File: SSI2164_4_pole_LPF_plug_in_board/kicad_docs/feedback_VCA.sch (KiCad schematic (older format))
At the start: 23 parts, among them Q3 BCM847DS135, Q4 MMBT3904, Q5 MMBT3904, Q6 MMBT3906, U5 TL072

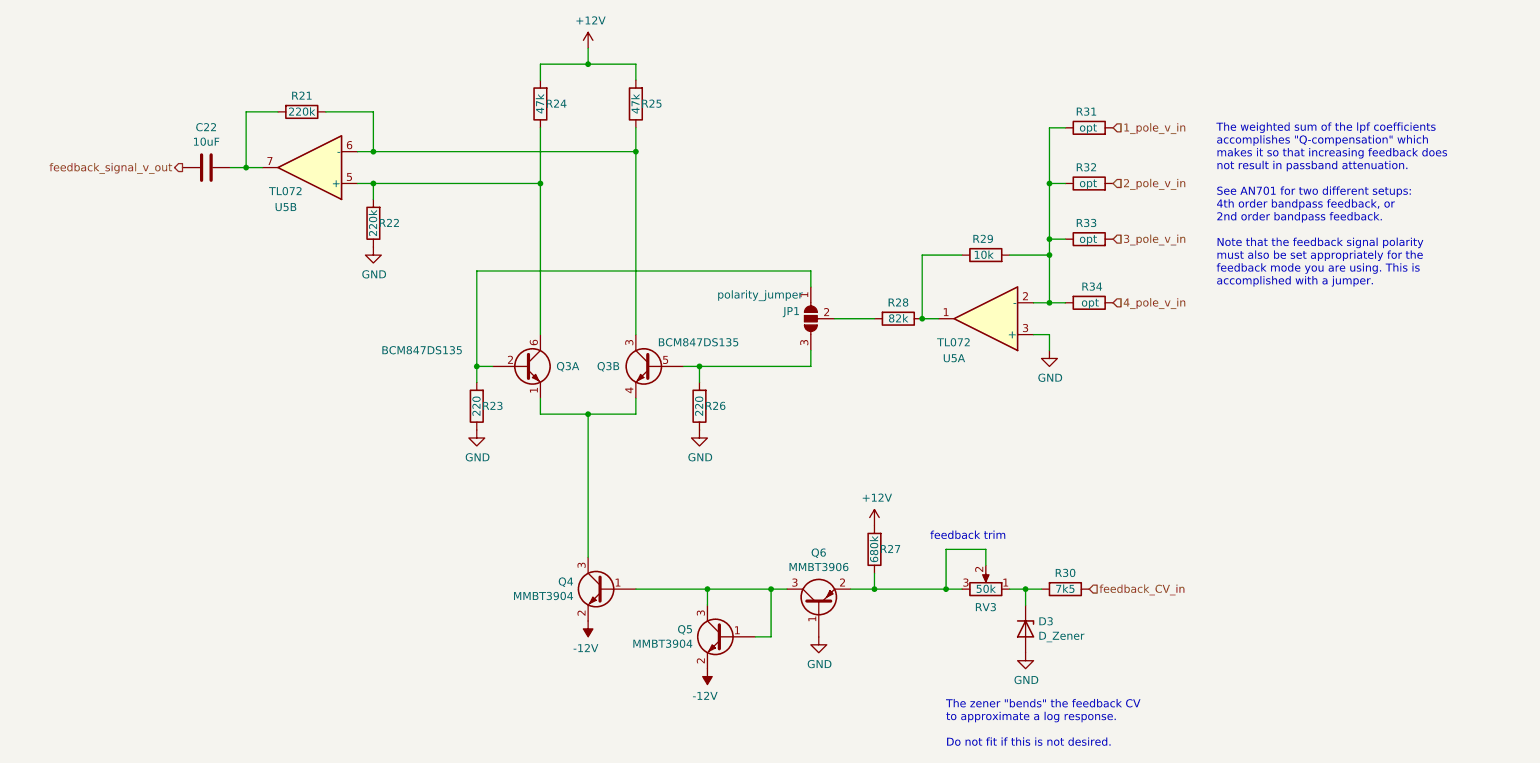
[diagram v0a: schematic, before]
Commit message: progress on SSI2164 LPF
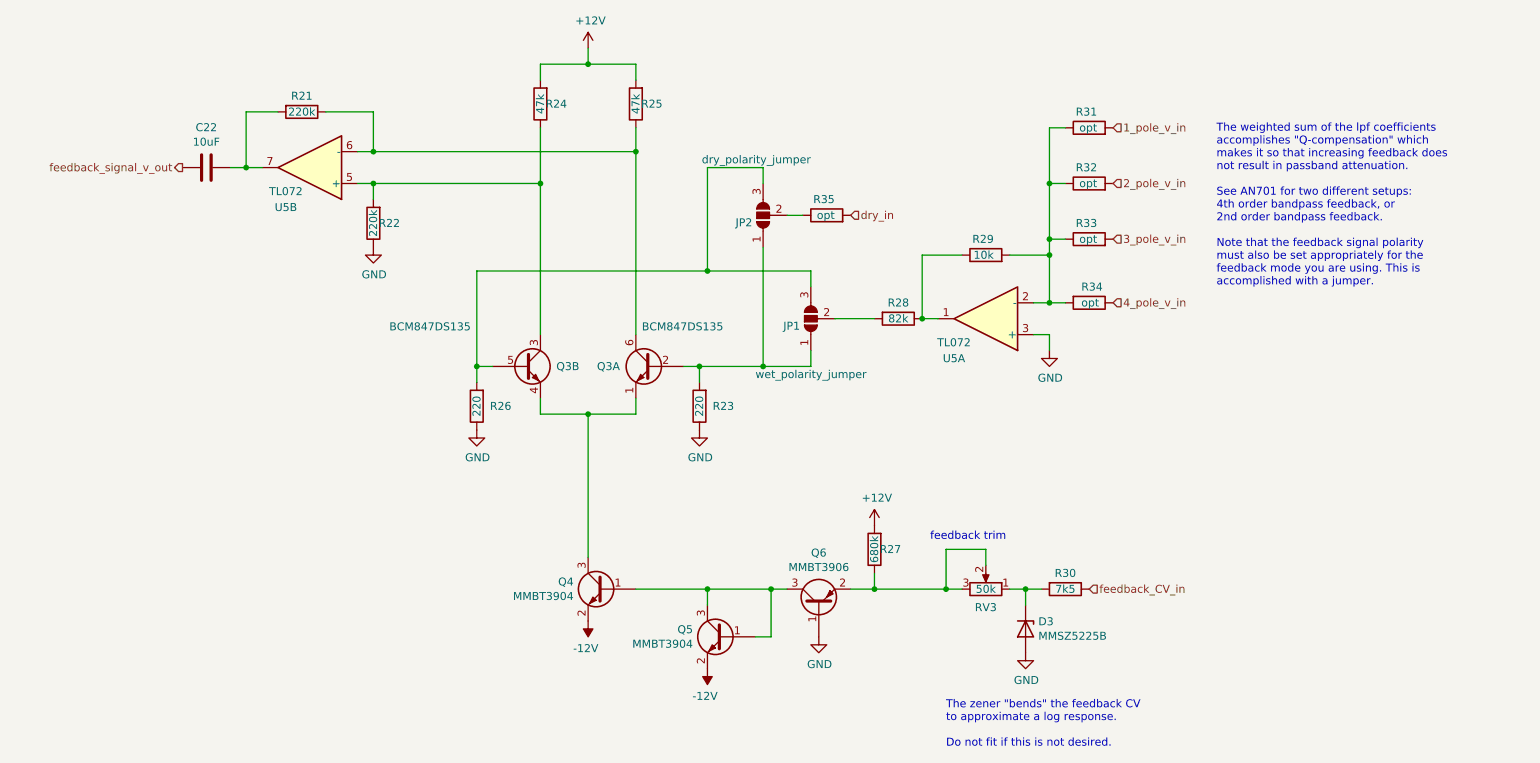
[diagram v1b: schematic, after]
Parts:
- added JP2: dry_polarity_jumper, Jumper:SolderJumper-3_P1.3mm_Open_RoundedPad1.0x1.5mm, symbol Jumper:SolderJumper_3_Open
- added R35: opt, Resistor_SMD:R_0805_2012Metric_Pad1.15x1.40mm_HandSolder, symbol Device:R
- C22: footprint Capacitor_THT:CP_Radial_D6.3mm_P2.50mm -> Capacitor_THT:C_Radial_D6.3mm_H5.0mm_P2.50mm
- D3: value D_Zener -> MMSZ5225B
- JP1: value polarity_jumper -> wet_polarity_jumper
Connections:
- net at R22.2, R24.1, U5.5 (+): now also Q3.3 (C); no longer Q3.6 (C)
- net at R21.1, R25.1, U5.6 (-): now also Q3.6 (C); no longer Q3.3 (C)
- net at JP1.1 (A), Q3.2 (B), R23.2: now also JP2.1 (A)
- net at JP1.3 (B), Q3.5 (B), R26.2: now also JP2.3 (B)
- new net: JP2.2 (C), R35.1
- new net dry_in: R35.2
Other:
- moved on the sheet: Q3A, Q3B, R23, R26
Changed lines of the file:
@@
 L Device:R R23
 U 1 1 5F0EDC2E
-P 4000 3700
-F 0 "R23" H 3900 3700 50  0000 C CNN
-F 1 "220" V 4000 3700 50  0000 C CNN
-F 2 "Resistor_SMD:R_0805_2012Metric_Pad1.15x1.40mm_HandSolder" V 3930 3700 50  0001 C CNN
-F 3 "~" H 4000 3700 50  0001 C CNN
-	1    4000 3700
+P 5400 3700
+F 0 "R23" H 5250 3700 50  0000 C CNN
+F 1 "220" V 5400 3700 50  0000 C CNN
+F 2 "Resistor_SMD:R_0805_2012Metric_Pad1.15x1.40mm_HandSolder" V 5330 3700 50  0001 C CNN
+F 3 "~" H 5400 3700 50  0001 C CNN
+	1    5400 3700
 	-1   0    0    1
 $EndComp
@@
 L Device:R R26
 U 1 1 5F0EEFAD
-P 5400 3700
-F 0 "R26" H 5300 3700 50  0000 C CNN
-F 1 "220" V 5400 3700 50  0000 C CNN
-F 2 "Resistor_SMD:R_0805_2012Metric_Pad1.15x1.40mm_HandSolder" V 5330 3700 50  0001 C CNN
-F 3 "~" H 5400 3700 50  0001 C CNN
-	1    5400 3700
+P 4000 3700
+F 0 "R26" H 3850 3700 50  0000 C CNN
+F 1 "220" V 4000 3700 50  0000 C CNN
+F 2 "Resistor_SMD:R_0805_2012Metric_Pad1.15x1.40mm_HandSolder" V 3930 3700 50  0001 C CNN
+F 3 "~" H 4000 3700 50  0001 C CNN
+	1    4000 3700
 	-1   0    0    1
 $EndComp
@@
 P 7450 5100
 F 0 "D3" V 7404 5180 50  0000 L CNN
-F 1 "D_Zener" V 7495 5180 50  0000 L CNN
+F 1 "MMSZ5225B" V 7495 5180 50  0000 L CNN
 F 2 "Diode_SMD:D_SOD-123" H 7450 5100 50  0001 C CNN
 F 3 "~" H 7450 5100 50  0001 C CNN
@@
 L lpf_parts:BCM847DS135 Q3
 U 1 1 5F114A19
+P 5100 3450
+F 0 "Q3" H 5300 3450 50  0000 L CNN
+F 1 "BCM847DS135" H 4650 3700 50  0000 L CNN
+F 2 "lpf_footprints:SOT457" H 5300 3375 50  0001 L CIN
+F 3 "" H 5100 3450 50  0001 L CNN
+	1    5100 3450
+	-1   0    0    -1
+$EndComp
+$Comp
+L lpf_parts:BCM847DS135 Q3
+U 2 1 5F12DDB3
 P 4300 3450
 F 0 "Q3" H 4500 3450 50  0000 L CNN
-F 1 "BCM847DS135" H 3400 3550 50  0000 L CNN
+F 1 "BCM847DS135" H 3450 3700 50  0000 L CNN
 F 2 "lpf_footprints:SOT457" H 4500 3375 50  0001 L CIN
 F 3 "" H 4300 3450 50  0001 L CNN
-	1    4300 3450
-	1    0    0    -1
-$EndComp
-$Comp
-L lpf_parts:BCM847DS135 Q3
-U 2 1 5F12DDB3
-P 5100 3450
-F 0 "Q3" H 5300 3450 50  0000 L CNN
-F 1 "BCM847DS135" H 4550 3600 50  0000 L CNN
-F 2 "lpf_footprints:SOT457" H 5300 3375 50  0001 L CIN
-F 3 "" H 5100 3450 50  0001 L CNN
-	2    5100 3450
-	-1   0    0    -1
+	2    4300 3450
+	1    0    0    -1
 $EndComp
 Wire Wire Line
@@
 Connection ~ 3350 2100
 Connection ~ 5000 2100
-Wire Wire Line
-	5000 2100 5000 3250
 Wire Wire Line
 	3350 2300 4400 2300
@@
 P 6100 3150
 F 0 "JP1" V 6054 3218 50  0000 L CNN
-F 1 "polarity_jumper" V 5950 3200 50  0000 L CNN
+F 1 "wet_polarity_jumper" V 5750 2800 50  0000 L CNN
 F 2 "Jumper:SolderJumper-3_P1.3mm_Open_RoundedPad1.0x1.5mm" H 6100 3150 50  0001 C CNN
 F 3 "~" H 6100 3150 50  0001 C CNN
 	1    6100 3150
-	0    -1   1    0
+	0    -1   -1   0
 $EndComp
 Wire Wire Line
 	6100 3350 6100 3450
 Wire Wire Line
-	6100 3450 5400 3450
+	6100 3450 5800 3450
 Connection ~ 5400 3450
 Wire Wire Line
 	6100 2950 6100 2850
 Wire Wire Line
-	6100 2850 4000 2850
+	6100 2850 5450 2850
 Text Notes 6850 4550 0    50   ~ 0
 feedback trim
@@
 F 0 "C22" V 2048 2200 50  0000 C CNN
 F 1 "10uF" V 2139 2200 50  0000 C CNN
-F 2 "Capacitor_THT:CP_Radial_D6.3mm_P2.50mm" H 2338 2050 50  0001 C CNN
+F 2 "Capacitor_THT:C_Radial_D6.3mm_H5.0mm_P2.50mm" H 2338 2050 50  0001 C CNN
 F 3 "~" H 2300 2200 50  0001 C CNN
 	1    2300 2200
 	0    1    1    0
 $EndComp
-Text Notes 8650 2950 0    50   ~ 0
-The weighted sum of the lpf coefficients\naccomplishes "Q-compensation" which\nmakes it so that increasing feedback does\nnot result in passband attenuation.\n\nSee AN701 for two different setups:\n4th order bandpass feedback, or\n2nd order bandpass feedback.\n\nNote that the feedback signal polarity\nmust also be set appropriately for the \nfeedback mode you are using. This is \naccomplished with a jumper.
 $Comp
 L Device:R R?
@@
 	0    -1   -1   0
 $EndComp
+Wire Wire Line
+	5000 2100 5000 3250
+Text Notes 8650 2950 0    50   ~ 0
+The weighted sum of the lpf coefficients\naccomplishes "Q-compensation" which\nmakes it so that increasing feedback does\nnot result in passband attenuation.\n\nSee AN701 for two different setups:\n4th order bandpass feedback, or\n2nd order bandpass feedback.\n\nNote that the feedback signal polarity\nmust also be set appropriately for the \nfeedback mode you are using. This is \naccomplished with a jumper.
+$Comp
+L Jumper:SolderJumper_3_Open JP2
+U 1 1 5F3B01D8
+P 5800 2500
+F 0 "JP2" V 5754 2568 50  0000 L CNN
+F 1 "dry_polarity_jumper" V 6150 2200 50  0000 L CNN
+F 2 "Jumper:SolderJumper-3_P1.3mm_Open_RoundedPad1.0x1.5mm" H 5800 2500 50  0001 C CNN
+F 3 "~" H 5800 2500 50  0001 C CNN
+	1    5800 2500
+	0    -1   -1   0
+$EndComp
+$Comp
+L Device:R R?
+U 1 1 5F3B1412
+P 6200 2500
+AR Path="/5EE91CC9/5F3B1412" Ref="R?"  Part="1"
+AR Path="/5F3B1412" Ref="R?"  Part="1"
+AR Path="/5F0B7B01/5F3B1412" Ref="R35"  Part="1"
+F 0 "R35" V 6300 2450 50  0000 L CNN
+F 1 "opt" V 6200 2450 50  0000 L CNN
+F 2 "Resistor_SMD:R_0805_2012Metric_Pad1.15x1.40mm_HandSolder" V 6130 2500 50  0001 C CNN
+F 3 "~" H 6200 2500 50  0001 C CNN
+	1    6200 2500
+	0    -1   -1   0
+$EndComp
+Wire Wire Line
+	5950 2500 6050 2500
+Text HLabel 6350 2500 2    50   Input ~ 0
+dry_in
+Wire Wire Line
+	5800 2700 5800 3450
+Connection ~ 5800 3450
+Wire Wire Line
+	5800 3450 5400 3450
+Wire Wire Line
+	5800 2300 5800 2200
+Wire Wire Line
+	5800 2200 5450 2200
+Wire Wire Line
+	5450 2200 5450 2850
+Connection ~ 5450 2850
+Wire Wire Line
+	5450 2850 4000 2850
 $EndSCHEMATC

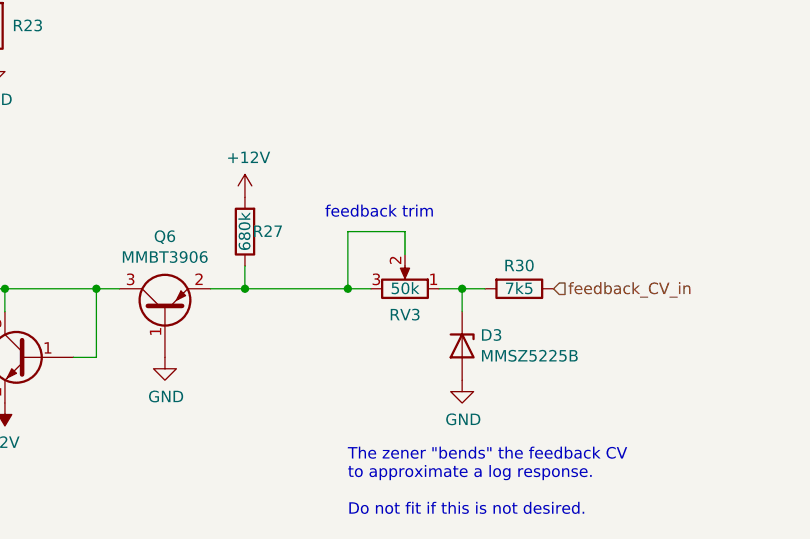
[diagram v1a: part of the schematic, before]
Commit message: flip trimpots for consistency
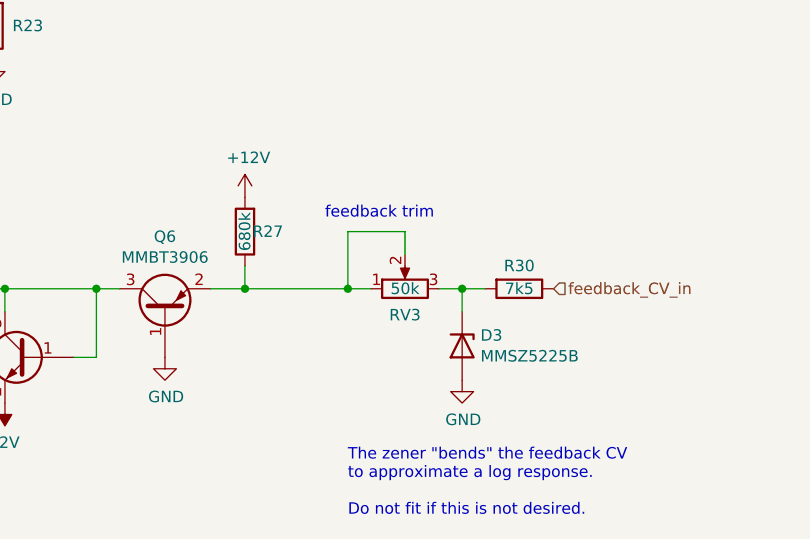
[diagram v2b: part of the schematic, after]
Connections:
- net at D3.1 (K), R30.2: now also RV3.3; no longer RV3.1
- net at Q6.2 (E), R27.1, RV3.2: now also RV3.1; no longer RV3.3
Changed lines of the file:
@@
 F 3 "~" H 7200 4850 50  0001 C CNN
 	1    7200 4850
-	0    1    -1   0
+	0    -1   -1   0
 $EndComp
 Wire Wire Line
